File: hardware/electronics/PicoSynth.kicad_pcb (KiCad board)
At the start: 2 copper layers, 28 parts, among them U1 Pico, U2 PCM5102A, U3 TC1262-33, U4 TC1262-33

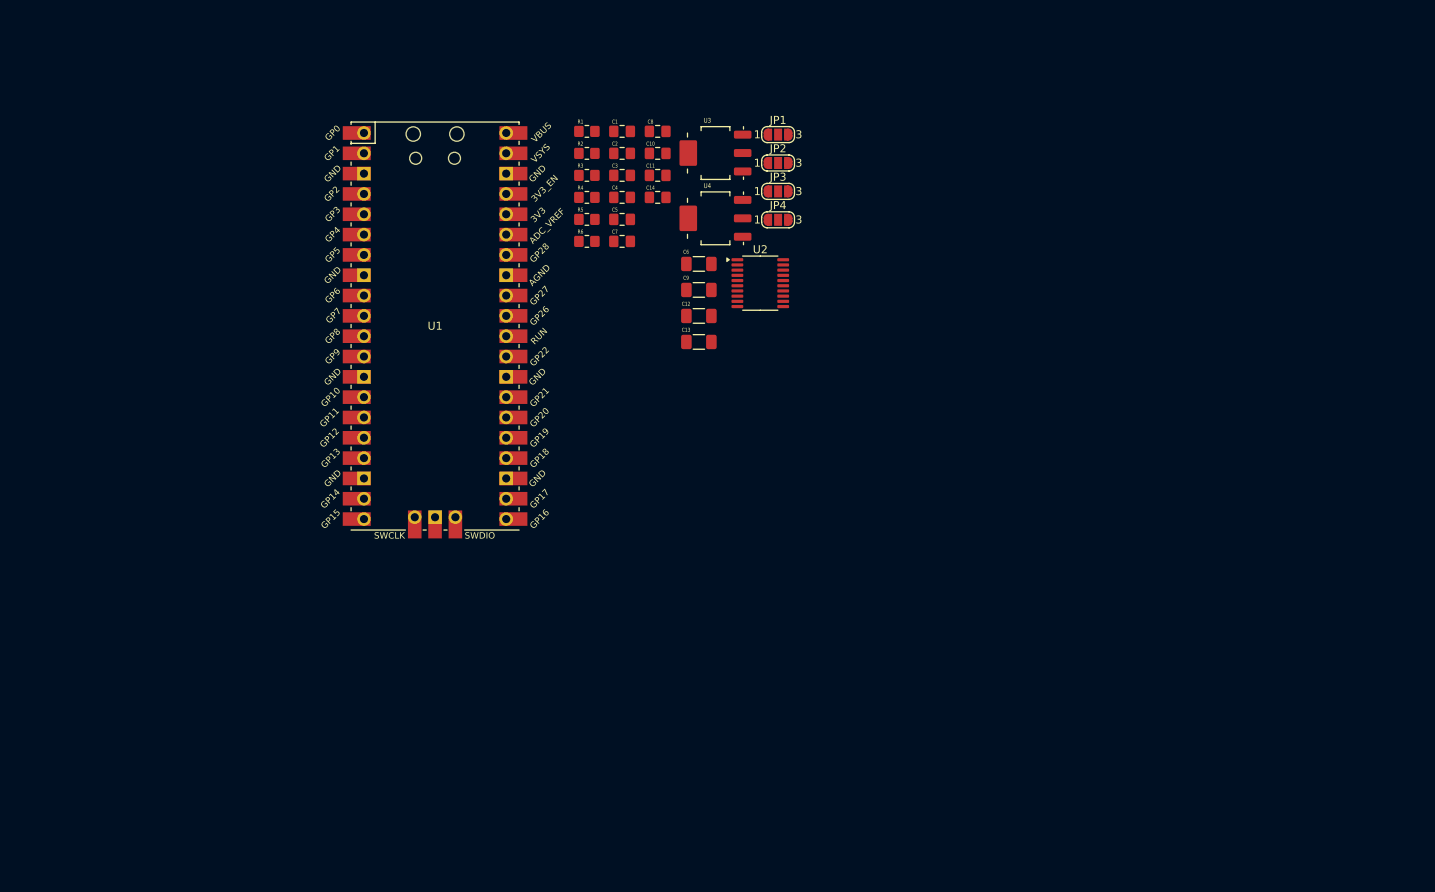
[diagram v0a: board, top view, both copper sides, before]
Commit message: A lot of updates in the Schematic... To-Do: hot swaps in switches, SD card and I2C for screen
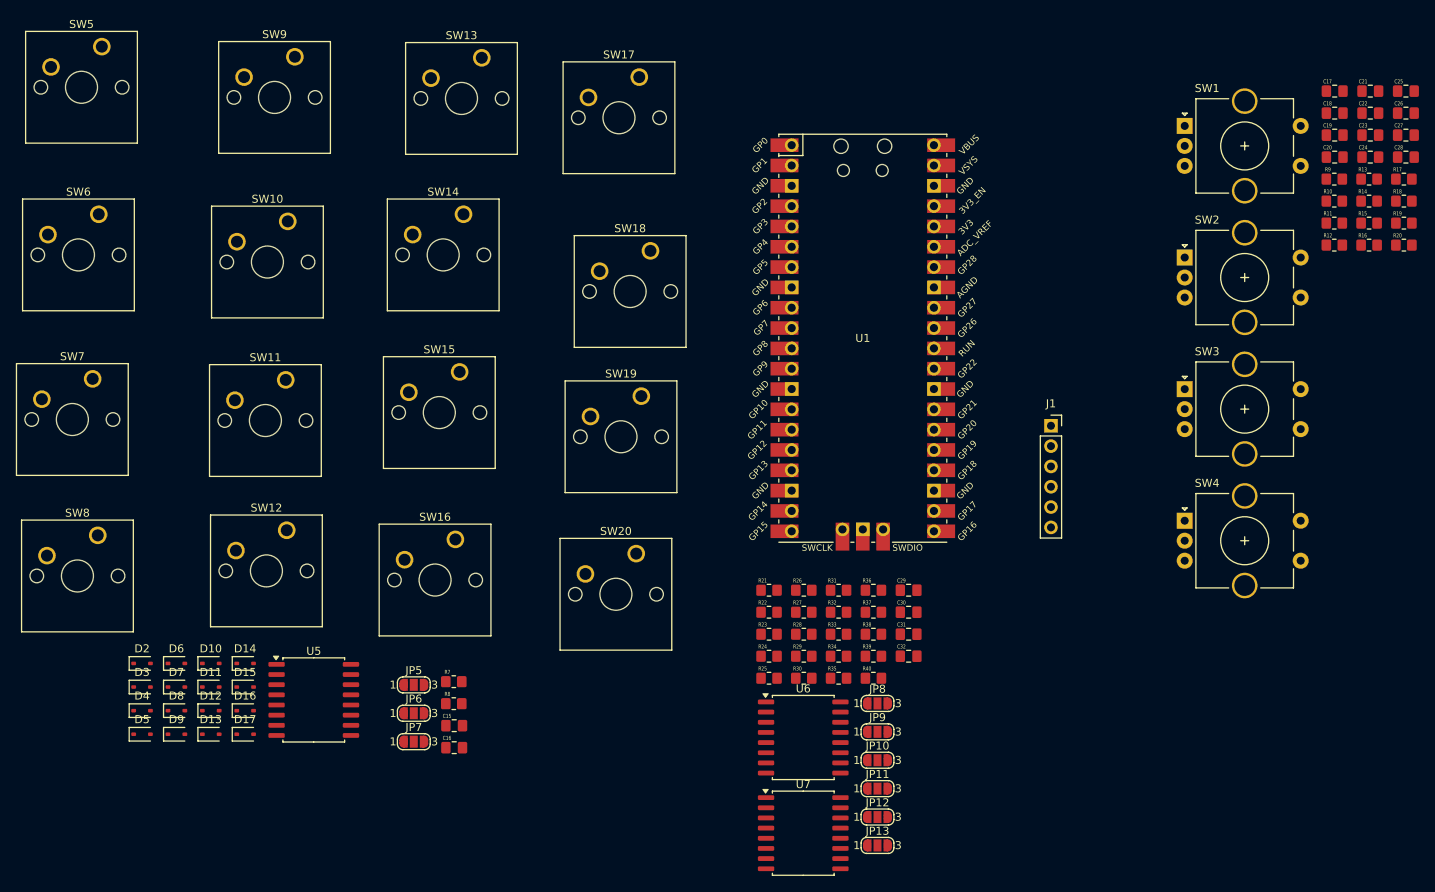
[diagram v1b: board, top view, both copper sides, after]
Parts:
- removed C1, C10, C2, C3, C4, C7: 2.2uF, Cern_Ignition:C_0805_2012Metric_Pad1.18x1.45mm_HandSolder_modif
- removed C11, C14, C5, C8: 100nF, Cern_Ignition:C_0805_2012Metric_Pad1.18x1.45mm_HandSolder_modif
- removed C12, C13, C6, C9: 10uF, Cern_Ignition:C_1206_3216Metric_Pad1.33x1.80mm_HandSolder_modif
- removed JP1: FLT_Jumper, Jumper:SolderJumper-3_P1.3mm_Open_RoundedPad1.0x1.5mm_NumberLabels
- removed JP2: DEMP_Jumper, Jumper:SolderJumper-3_P1.3mm_Open_RoundedPad1.0x1.5mm_NumberLabels
- removed JP3: XMST_Jumper, Jumper:SolderJumper-3_P1.3mm_Open_RoundedPad1.0x1.5mm_NumberLabels
- removed JP4: FMT_Jumper, Jumper:SolderJumper-3_P1.3mm_Open_RoundedPad1.0x1.5mm_NumberLabels
- removed R1, R2: 470R, Cern_Ignition:R_0805_2012Metric_Pad1.20x1.40mm_HandSolder_modif
- removed R3: 1k, Cern_Ignition:R_0805_2012Metric_Pad1.20x1.40mm_HandSolder_modif
- removed R4, R5, R6: 22R, Cern_Ignition:R_0805_2012Metric_Pad1.20x1.40mm_HandSolder_modif
- removed U2: PCM5102A, Package_SO:TSSOP-20_4.4x6.5mm_P0.65mm
- removed U3, U4: TC1262-33, Cern_Ignition:SOT-223_modif_1L
- added C15: 100nF, Cern_Ignition:C_0805_2012Metric_Pad1.18x1.45mm_HandSolder_modif, F.Cu at (82.5, 109.8)
- added C16: 2.2uF, Cern_Ignition:C_0805_2012Metric_Pad1.18x1.45mm_HandSolder_modif, F.Cu at (82.5, 112.5)
- added C17: 100nF, Cern_Ignition:C_0805_2012Metric_Pad1.18x1.45mm_HandSolder_modif, F.Cu at (192.6, 30.5)
- added C18: 100nF, Cern_Ignition:C_0805_2012Metric_Pad1.18x1.45mm_HandSolder_modif, F.Cu at (192.6, 33.2)
- added C19: 100nF, Cern_Ignition:C_0805_2012Metric_Pad1.18x1.45mm_HandSolder_modif, F.Cu at (192.6, 36.0)
- added C20: 100nF, Cern_Ignition:C_0805_2012Metric_Pad1.18x1.45mm_HandSolder_modif, F.Cu at (192.6, 38.7)
- added C21: 100nF, Cern_Ignition:C_0805_2012Metric_Pad1.18x1.45mm_HandSolder_modif, F.Cu at (197.0, 30.5)
- added C22: 100nF, Cern_Ignition:C_0805_2012Metric_Pad1.18x1.45mm_HandSolder_modif, F.Cu at (197.0, 33.2)
- added C23: 100nF, Cern_Ignition:C_0805_2012Metric_Pad1.18x1.45mm_HandSolder_modif, F.Cu at (197.0, 36.0)
- added C24: 100nF, Cern_Ignition:C_0805_2012Metric_Pad1.18x1.45mm_HandSolder_modif, F.Cu at (197.0, 38.7)
- added C25: 100nF, Cern_Ignition:C_0805_2012Metric_Pad1.18x1.45mm_HandSolder_modif, F.Cu at (201.5, 30.5)
- added C26: 100nF, Cern_Ignition:C_0805_2012Metric_Pad1.18x1.45mm_HandSolder_modif, F.Cu at (201.5, 33.2)
- added C27: 100nF, Cern_Ignition:C_0805_2012Metric_Pad1.18x1.45mm_HandSolder_modif, F.Cu at (201.5, 36.0)
- added C28: 100nF, Cern_Ignition:C_0805_2012Metric_Pad1.18x1.45mm_HandSolder_modif, F.Cu at (201.5, 38.7)
- added C29: 2.2uF, Cern_Ignition:C_0805_2012Metric_Pad1.18x1.45mm_HandSolder_modif, F.Cu at (139.3, 92.8)
- added C30: 100nF, Cern_Ignition:C_0805_2012Metric_Pad1.18x1.45mm_HandSolder_modif, F.Cu at (139.3, 95.6)
- added C31: 2.2uF, Cern_Ignition:C_0805_2012Metric_Pad1.18x1.45mm_HandSolder_modif, F.Cu at (139.3, 98.3)
- added C32: 100nF, Cern_Ignition:C_0805_2012Metric_Pad1.18x1.45mm_HandSolder_modif, F.Cu at (139.3, 101.1)
- added D10: 1N4148WS, Diode_SMD:D_SOD-323, F.Cu at (52.1, 102.0)
- added D11: 1N4148WS, Diode_SMD:D_SOD-323, F.Cu at (52.1, 104.9)
- added D12: 1N4148WS, Diode_SMD:D_SOD-323, F.Cu at (52.1, 107.9)
- added D13: 1N4148WS, Diode_SMD:D_SOD-323, F.Cu at (52.1, 110.8)
- added D14: 1N4148WS, Diode_SMD:D_SOD-323, F.Cu at (56.4, 102.0)
- added D15: 1N4148WS, Diode_SMD:D_SOD-323, F.Cu at (56.4, 104.9)
- added D16: 1N4148WS, Diode_SMD:D_SOD-323, F.Cu at (56.4, 107.9)
- added D17: 1N4148WS, Diode_SMD:D_SOD-323, F.Cu at (56.4, 110.8)
- added D2: 1N4148WS, Diode_SMD:D_SOD-323, F.Cu at (43.5, 102.0)
- added D3: 1N4148WS, Diode_SMD:D_SOD-323, F.Cu at (43.5, 104.9)
- added D4: 1N4148WS, Diode_SMD:D_SOD-323, F.Cu at (43.5, 107.9)
- added D5: 1N4148WS, Diode_SMD:D_SOD-323, F.Cu at (43.5, 110.8)
- added D6: 1N4148WS, Diode_SMD:D_SOD-323, F.Cu at (47.8, 102.0)
- added D7: 1N4148WS, Diode_SMD:D_SOD-323, F.Cu at (47.8, 104.9)
- added D8: 1N4148WS, Diode_SMD:D_SOD-323, F.Cu at (47.8, 107.9)
- added D9: 1N4148WS, Diode_SMD:D_SOD-323, F.Cu at (47.8, 110.8)
- added J1: Conn_01x06_Socket, Connector_PinSocket_2.54mm:PinSocket_1x06_P2.54mm_Vertical, F.Cu at (157.1, 72.3)
- added JP10: FLT_Jumper, Jumper:SolderJumper-3_P1.3mm_Open_RoundedPad1.0x1.5mm_NumberLabels, F.Cu at (135.4, 114.1)
- added JP11: FLT_Jumper, Jumper:SolderJumper-3_P1.3mm_Open_RoundedPad1.0x1.5mm_NumberLabels, F.Cu at (135.4, 117.6)
- added JP12: FLT_Jumper, Jumper:SolderJumper-3_P1.3mm_Open_RoundedPad1.0x1.5mm_NumberLabels, F.Cu at (135.4, 121.2)
- added JP13: FLT_Jumper, Jumper:SolderJumper-3_P1.3mm_Open_RoundedPad1.0x1.5mm_NumberLabels, F.Cu at (135.4, 124.7)
- added JP5: FLT_Jumper, Jumper:SolderJumper-3_P1.3mm_Open_RoundedPad1.0x1.5mm_NumberLabels, F.Cu at (77.5, 104.7)
- added JP6: FLT_Jumper, Jumper:SolderJumper-3_P1.3mm_Open_RoundedPad1.0x1.5mm_NumberLabels, F.Cu at (77.5, 108.2)
- added JP7: FLT_Jumper, Jumper:SolderJumper-3_P1.3mm_Open_RoundedPad1.0x1.5mm_NumberLabels, F.Cu at (77.5, 111.8)
- added JP8: FLT_Jumper, Jumper:SolderJumper-3_P1.3mm_Open_RoundedPad1.0x1.5mm_NumberLabels, F.Cu at (135.4, 107.0)
- added JP9: FLT_Jumper, Jumper:SolderJumper-3_P1.3mm_Open_RoundedPad1.0x1.5mm_NumberLabels, F.Cu at (135.4, 110.5)
- added R10: 1k, Cern_Ignition:R_0805_2012Metric_Pad1.20x1.40mm_HandSolder_modif, F.Cu at (192.5, 44.2)
- added R11: 1k, Cern_Ignition:R_0805_2012Metric_Pad1.20x1.40mm_HandSolder_modif, F.Cu at (192.5, 47.0)
- added R12: 1k, Cern_Ignition:R_0805_2012Metric_Pad1.20x1.40mm_HandSolder_modif, F.Cu at (192.5, 49.7)
- added R13: 1k, Cern_Ignition:R_0805_2012Metric_Pad1.20x1.40mm_HandSolder_modif, F.Cu at (196.9, 41.5)
- added R14: 1k, Cern_Ignition:R_0805_2012Metric_Pad1.20x1.40mm_HandSolder_modif, F.Cu at (196.9, 44.2)
- added R15: 1k, Cern_Ignition:R_0805_2012Metric_Pad1.20x1.40mm_HandSolder_modif, F.Cu at (196.9, 47.0)
- added R16: 1k, Cern_Ignition:R_0805_2012Metric_Pad1.20x1.40mm_HandSolder_modif, F.Cu at (196.9, 49.7)
- added R17: 1k, Cern_Ignition:R_0805_2012Metric_Pad1.20x1.40mm_HandSolder_modif, F.Cu at (201.2, 41.5)
- added R18: 1k, Cern_Ignition:R_0805_2012Metric_Pad1.20x1.40mm_HandSolder_modif, F.Cu at (201.2, 44.2)
- added R19: 1k, Cern_Ignition:R_0805_2012Metric_Pad1.20x1.40mm_HandSolder_modif, F.Cu at (201.2, 47.0)
- added R20: 1k, Cern_Ignition:R_0805_2012Metric_Pad1.20x1.40mm_HandSolder_modif, F.Cu at (201.2, 49.7)
- added R21: 4.7k, Cern_Ignition:R_0805_2012Metric_Pad1.20x1.40mm_HandSolder_modif, F.Cu at (121.9, 92.8)
- added R22: 4.7k, Cern_Ignition:R_0805_2012Metric_Pad1.20x1.40mm_HandSolder_modif, F.Cu at (121.9, 95.6)
- added R23: 1k, Cern_Ignition:R_0805_2012Metric_Pad1.20x1.40mm_HandSolder_modif, F.Cu at (121.9, 98.3)
- added R24: 1k, Cern_Ignition:R_0805_2012Metric_Pad1.20x1.40mm_HandSolder_modif, F.Cu at (121.9, 101.1)
- added R25: 1k, Cern_Ignition:R_0805_2012Metric_Pad1.20x1.40mm_HandSolder_modif, F.Cu at (121.9, 103.8)
- added R26: 1k, Cern_Ignition:R_0805_2012Metric_Pad1.20x1.40mm_HandSolder_modif, F.Cu at (126.2, 92.8)
- added R27: 1k, Cern_Ignition:R_0805_2012Metric_Pad1.20x1.40mm_HandSolder_modif, F.Cu at (126.2, 95.6)
- added R28: 1k, Cern_Ignition:R_0805_2012Metric_Pad1.20x1.40mm_HandSolder_modif, F.Cu at (126.2, 98.3)
- added R29: 1k, Cern_Ignition:R_0805_2012Metric_Pad1.20x1.40mm_HandSolder_modif, F.Cu at (126.2, 101.1)
- added R30: 1k, Cern_Ignition:R_0805_2012Metric_Pad1.20x1.40mm_HandSolder_modif, F.Cu at (126.2, 103.8)
- added R31: 4.7k, Cern_Ignition:R_0805_2012Metric_Pad1.20x1.40mm_HandSolder_modif, F.Cu at (130.6, 92.8)
- added R32: 4.7k, Cern_Ignition:R_0805_2012Metric_Pad1.20x1.40mm_HandSolder_modif, F.Cu at (130.6, 95.6)
- added R33: 1k, Cern_Ignition:R_0805_2012Metric_Pad1.20x1.40mm_HandSolder_modif, F.Cu at (130.6, 98.3)
- added R34: 1k, Cern_Ignition:R_0805_2012Metric_Pad1.20x1.40mm_HandSolder_modif, F.Cu at (130.6, 101.1)
- added R35: 1k, Cern_Ignition:R_0805_2012Metric_Pad1.20x1.40mm_HandSolder_modif, F.Cu at (130.6, 103.8)
- added R36: 1k, Cern_Ignition:R_0805_2012Metric_Pad1.20x1.40mm_HandSolder_modif, F.Cu at (134.9, 92.8)
- added R37: 1k, Cern_Ignition:R_0805_2012Metric_Pad1.20x1.40mm_HandSolder_modif, F.Cu at (134.9, 95.6)
- added R38: 1k, Cern_Ignition:R_0805_2012Metric_Pad1.20x1.40mm_HandSolder_modif, F.Cu at (134.9, 98.3)
- added R39: 1k, Cern_Ignition:R_0805_2012Metric_Pad1.20x1.40mm_HandSolder_modif, F.Cu at (134.9, 101.1)
- added R40: 1k, Cern_Ignition:R_0805_2012Metric_Pad1.20x1.40mm_HandSolder_modif, F.Cu at (134.9, 103.8)
- added R7: 4.7k, Cern_Ignition:R_0805_2012Metric_Pad1.20x1.40mm_HandSolder_modif, F.Cu at (82.5, 104.3)
- added R8: 4.7k, Cern_Ignition:R_0805_2012Metric_Pad1.20x1.40mm_HandSolder_modif, F.Cu at (82.5, 107.0)
- added R9: 1k, Cern_Ignition:R_0805_2012Metric_Pad1.20x1.40mm_HandSolder_modif, F.Cu at (192.5, 41.5)
- added SW1: RotaryEncoder_Switch_MP, Rotary_Encoder:RotaryEncoder_Alps_EC11E-Switch_Vertical_H20mm_CircularMountingHoles, F.Cu at (173.8, 34.8)
- added SW10: SW_Push_45deg, Lame_Lib:SW_Cherry_MX_1.00u_PCB, F.Cu at (61.7, 46.7)
- added SW11: SW_Push_45deg, Lame_Lib:SW_Cherry_MX_1.00u_PCB, F.Cu at (61.5, 66.5)
- added SW12: SW_Push_45deg, Lame_Lib:SW_Cherry_MX_1.00u_PCB, F.Cu at (61.6, 85.3)
- added SW13: SW_Push_45deg, Lame_Lib:SW_Cherry_MX_1.00u_PCB, F.Cu at (86.0, 26.3)
- added SW14: SW_Push_45deg, Lame_Lib:SW_Cherry_MX_1.00u_PCB, F.Cu at (83.7, 45.8)
- added SW15: SW_Push_45deg, Lame_Lib:SW_Cherry_MX_1.00u_PCB, F.Cu at (83.2, 65.6)
- added SW16: SW_Push_45deg, Lame_Lib:SW_Cherry_MX_1.00u_PCB, F.Cu at (82.7, 86.5)
- added SW17: SW_Push_45deg, Lame_Lib:SW_Cherry_MX_1.00u_PCB, F.Cu at (105.7, 28.7)
- added SW18: SW_Push_45deg, Lame_Lib:SW_Cherry_MX_1.00u_PCB, F.Cu at (107.1, 50.4)
- added SW19: SW_Push_45deg, Lame_Lib:SW_Cherry_MX_1.00u_PCB, F.Cu at (105.9, 68.6)
- added SW2: RotaryEncoder_Switch_MP, Rotary_Encoder:RotaryEncoder_Alps_EC11E-Switch_Vertical_H20mm_CircularMountingHoles, F.Cu at (173.8, 51.3)
- added SW20: SW_Push_45deg, Lame_Lib:SW_Cherry_MX_1.00u_PCB, F.Cu at (105.3, 88.3)
- added SW3: RotaryEncoder_Switch_MP, Rotary_Encoder:RotaryEncoder_Alps_EC11E-Switch_Vertical_H20mm_CircularMountingHoles, F.Cu at (173.8, 67.7)
- added SW4: RotaryEncoder_Switch_MP, Rotary_Encoder:RotaryEncoder_Alps_EC11E-Switch_Vertical_H20mm_CircularMountingHoles, F.Cu at (173.8, 84.2)
- added SW5: SW_Push_45deg, Lame_Lib:SW_Cherry_MX_1.00u_PCB, F.Cu at (38.5, 24.9)
- added SW6: SW_Push_45deg, Lame_Lib:SW_Cherry_MX_1.00u_PCB, F.Cu at (38.1, 45.8)
- added SW7: SW_Push_45deg, Lame_Lib:SW_Cherry_MX_1.00u_PCB, F.Cu at (37.3, 66.4)
- added SW8: SW_Push_45deg, Lame_Lib:SW_Cherry_MX_1.00u_PCB, F.Cu at (38.0, 86.0)
- added SW9: SW_Push_45deg, Lame_Lib:SW_Cherry_MX_1.00u_PCB, F.Cu at (62.6, 26.2)
- added U5: PCF8574, Package_SO:SOIC-16W_7.5x10.3mm_P1.27mm, F.Cu at (65.0, 106.6)
- added U6: PCF8574, Package_SO:SOIC-16W_7.5x10.3mm_P1.27mm, F.Cu at (126.2, 111.3)
- added U7: PCF8574, Package_SO:SOIC-16W_7.5x10.3mm_P1.27mm, F.Cu at (126.2, 123.2)
- moved U1 53.5 mm to (133.6, 61.3)
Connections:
- U1 pad 16: unconnected-(U1-GPIO12-Pad16) -> /SDA_Bus_0
- U1 pad 17: unconnected-(U1-GPIO13-Pad17) -> /SCL_Bus_0
- U1 pad 19: unconnected-(U1-GPIO14-Pad19) -> /SDA_Bus_1
- U1 pad 20: unconnected-(U1-GPIO15-Pad20) -> /SCL_Bus_1
- U1 pad 36: unconnected-(U1-3V3-Pad36) -> /+3V3
